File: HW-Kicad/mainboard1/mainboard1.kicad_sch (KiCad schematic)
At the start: 58 parts, among them J1 Conn_01x04_Male, J2 Conn_01x02_Male, J3 Conn_01x07_Male, J4 Conn_01x04_Male, J5 Conn_01x04_Male, J8 Conn_02x10_Odd_Even, Q1 BC337, Q2 IRF9540N, Q3 BC337, Q4 BC337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

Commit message: agegue el conector de energía separado para el aprs
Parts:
- added J6: Conn_01x02_Male, Connector_PinHeader_2.54mm:PinHeader_1x02_P2.54mm_Vertical, symbol Connector:Conn_01x02_Male
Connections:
- net GND: now also J6.2 (Pin_2)
- net VBAT: no longer J2.1 (Pin_1)
- new net APRSBATT: J2.1 (Pin_1), J6.1 (Pin_1)
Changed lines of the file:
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@@
     (stroke (width 0) (type default) (color 0 0 0 0))
   )
-  (polyline (pts (xy 15.24 45.72) (xy 15.24 63.5))
+  (polyline (pts (xy 15.24 30.48) (xy 15.24 63.5))
     (stroke (width 0) (type default) (color 0 0 0 0))
   )
@@
     (stroke (width 0) (type default) (color 0 0 0 0))
   )
-  (polyline (pts (xy 41.91 45.72) (xy 46.99 45.72))
+  (polyline (pts (xy 42.545 30.48) (xy 46.99 30.48))
     (stroke (width 0) (type default) (color 0 0 0 0))
   )
@@
     (stroke (width 0) (type default) (color 0 0 0 0))
   )
-  (polyline (pts (xy 15.24 45.72) (xy 41.91 45.72))
+  (polyline (pts (xy 15.24 30.48) (xy 42.545 30.48))
     (stroke (width 0) (type default) (color 0 0 0 0))
   )
@@
     (stroke (width 0) (type default) (color 0 0 0 0))
   )
-  (polyline (pts (xy 46.99 60.96) (xy 46.99 45.72))
+  (polyline (pts (xy 46.99 60.96) (xy 46.99 30.48))
     (stroke (width 0) (type default) (color 0 0 0 0))
   )
@@
     (effects (font (size 1.27 1.27)) (justify left bottom))
   )
-  (text "Battery Module Input" (at 15.24 45.72 0)
+  (text "Battery Module Input" (at 16.51 16.51 0)
     (effects (font (size 1.27 1.27)) (justify left bottom))
   )
@@
     (effects (font (size 1.27 1.27)) (justify left bottom))
   )
-  (text "4,5 to 10v max" (at 44.45 160.02 0)
+  (text "4,5 to 10v max" (at 44.45 162.56 0)
     (effects (font (size 1.27 1.27)) (justify left bottom))
   )
@@
     )
   )
+  (global_label "APRSBATT" (shape input) (at 29.845 37.465 0) (fields_autoplaced)
+    (effects (font (size 1.27 1.27)) (justify left))
+    (property "Intersheet References" "${INTERSHEET_REFS}" (id 0) (at 41.39 37.3856 0)
+      (effects (font (size 1.27 1.27)) (justify left) hide)
+    )
+  )
   (global_label "SCL" (shape input) (at 128.27 129.54 180) (fields_autoplaced)
     (effects (font (size 1.27 1.27)) (justify right))
@@
     )
   )
-  (global_label "VBAT" (shape input) (at 36.83 158.75 0) (fields_autoplaced)
-    (effects (font (size 1.27 1.27)) (justify left))
-    (property "Intersheet References" "${INTERSHEET_REFS}" (id 0) (at 43.6579 158.6706 0)
-      (effects (font (size 1.27 1.27)) (justify left) hide)
-    )
-  )
   (global_label "PAYLOAD1RX" (shape input) (at 93.98 180.34 0) (fields_autoplaced)
     (effects (font (size 1.27 1.27)) (justify left))
@@
     (effects (font (size 1.27 1.27)) (justify left))
     (property "Intersheet References" "${INTERSHEET_REFS}" (id 0) (at 110.1212 185.4994 0)
+      (effects (font (size 1.27 1.27)) (justify left) hide)
+    )
+  )
+  (global_label "APRSBATT" (shape input) (at 36.83 158.75 0) (fields_autoplaced)
+    (effects (font (size 1.27 1.27)) (justify left))
+    (property "Intersheet References" "${INTERSHEET_REFS}" (id 0) (at 48.375 158.6706 0)
       (effects (font (size 1.27 1.27)) (justify left) hide)
     )
@@
     (pin "2")
     (pin "3")
+    (pin "5")
+    (pin "6")
+    (pin "7")
+    (pin "10")
+    (pin "8")
+    (pin "9")
+    (pin "12")
+    (pin "13")
+    (pin "14")
+    (pin "11")
+    (pin "4")
   )
   (symbol (lib_id "Device:R") (at 358.14 87.63 90) (unit 1)
@@
       (effects (font (size 1.27 1.27)) hide)
     )
+    (pin "1")
+    (pin "2")
+    (pin "3")
+    (pin "4")
+    (pin "5")
+    (pin "6")
+    (pin "10")
+    (pin "8")
+    (pin "9")
     (pin "11")
     (pin "12")
     (pin "13")
+    (pin "14")
+    (pin "7")
   )
   (symbol (lib_id "lm2596:YAAJ_DCDC_StepDown_LM2596") (at 72.39 54.61 0) (unit 1)
@@
       (effects (font (size 1.27 1.27)) hide)
     )
+    (pin "1")
+    (pin "2")
+    (pin "3")
     (pin "4")
     (pin "5")
     (pin "6")
+    (pin "10")
+    (pin "8")
+    (pin "9")
+    (pin "11")
+    (pin "12")
+    (pin "13")
+    (pin "14")
+    (pin "7")
   )
   (symbol (lib_id "power:GND") (at 273.05 234.95 0) (unit 1)
@@
       (effects (font (size 1.27 1.27)) hide)
     )
+    (pin "1")
+    (pin "2")
+    (pin "3")
+    (pin "4")
+    (pin "5")
+    (pin "6")
+    (pin "10")
+    (pin "8")
+    (pin "9")
+    (pin "11")
+    (pin "12")
+    (pin "13")
     (pin "14")
     (pin "7")
@@
       (effects (font (size 1.27 1.27)) hide)
     )
+    (pin "1")
+    (pin "2")
+    (pin "3")
+    (pin "5")
+    (pin "6")
+    (pin "7")
+    (pin "10")
+    (pin "8")
+    (pin "9")
+    (pin "12")
+    (pin "13")
+    (pin "14")
     (pin "11")
     (pin "4")
@@
       (effects (font (size 1.27 1.27)) hide)
     )
+    (pin "1")
+    (pin "2")
+    (pin "3")
     (pin "5")
     (pin "6")
     (pin "7")
+    (pin "10")
+    (pin "8")
+    (pin "9")
+    (pin "12")
+    (pin "13")
+    (pin "14")
+    (pin "11")
+    (pin "4")
   )
   (symbol (lib_id "Connector:Conn_01x02_Male") (at 31.75 158.75 0) (unit 1)
@@
     (pin "2")
     (pin "3")
+    (pin "4")
+    (pin "5")
+    (pin "6")
+    (pin "10")
+    (pin "8")
+    (pin "9")
+    (pin "11")
+    (pin "12")
+    (pin "13")
+    (pin "14")
+    (pin "7")
   )
   (symbol (lib_id "Device:C") (at 369.57 181.61 90) (unit 1)
@@
       (effects (font (size 1.27 1.27)) hide)
     )
+    (pin "1")
+    (pin "2")
+    (pin "3")
+    (pin "5")
+    (pin "6")
+    (pin "7")
+    (pin "10")
+    (pin "8")
+    (pin "9")
     (pin "12")
     (pin "13")
     (pin "14")
+    (pin "11")
+    (pin "4")
   )
   (symbol (lib_id "Device:R") (at 375.92 189.23 180) (unit 1)
@@
     (pin "1")
     (pin "2")
+  )
+  (symbol (lib_id "power:GND") (at 29.845 40.005 0) (unit 1)
+    (in_bom yes) (on_board yes)
+    (property "Reference" "#PWR0133" (id 0) (at 29.845 46.355 0)
+      (effects (font (size 1.27 1.27)) hide)
+    )
+    (property "Value" "GND" (id 1) (at 33.02 42.545 0))
+    (property "Footprint" "" (id 2) (at 29.845 40.005 0)
+      (effects (font (size 1.27 1.27)) hide)
+    )
+    (property "Datasheet" "" (id 3) (at 29.845 40.005 0)
+      (effects (font (size 1.27 1.27)) hide)
+    )
+    (pin "1")
   )
   (symbol (lib_id "power:GND") (at 251.46 109.22 0) (unit 1)
@@
     (pin "2")
   )
+  (symbol (lib_id "Connector:Conn_01x02_Male") (at 24.765 37.465 0) (unit 1)
+    (in_bom yes) (on_board yes) (fields_autoplaced)
+    (property "Reference" "J6" (id 0) (at 25.4 32.385 0))
+    (property "Value" "Conn_01x02_Male" (id 1) (at 25.4 34.925 0))
+    (property "Footprint" "Connector_PinHeader_2.54mm:PinHeader_1x02_P2.54mm_Vertical" (id 2) (at 24.765 37.465 0)
+      (effects (font (size 1.27 1.27)) hide)
+    )
+    (property "Datasheet" "~" (id 3) (at 24.765 37.465 0)
+      (effects (font (size 1.27 1.27)) hide)
+    )
+    (pin "1")
+    (pin "2")
+  )
   (symbol (lib_id "power:GND") (at 264.16 81.28 0) (unit 1)
     (in_bom yes) (on_board yes) (fields_autoplaced)
@@
       (effects (font (size 1.27 1.27)) hide)
     )
+    (pin "1")
+    (pin "2")
+    (pin "3")
+    (pin "4")
+    (pin "5")
+    (pin "6")
     (pin "10")
     (pin "8")
     (pin "9")
+    (pin "11")
+    (pin "12")
+    (pin "13")
+    (pin "14")
+    (pin "7")
   )
   (symbol (lib_id "power:GND") (at 199.39 147.32 0) (unit 1)
@@
       (effects (font (size 1.27 1.27)) hide)
     )
+    (pin "1")
+    (pin "2")
+    (pin "3")
+    (pin "5")
+    (pin "6")
+    (pin "7")
     (pin "10")
     (pin "8")
     (pin "9")
+    (pin "12")
+    (pin "13")
+    (pin "14")
+    (pin "11")
+    (pin "4")
   )
   (symbol (lib_id "Device:C") (at 273.05 104.14 0) (unit 1)
@@
       (reference "#PWR0132") (unit 1) (value "GND") (footprint "")
     )
+    (path "/9f20b7bf-a242-4e3a-9aaa-c06982823dd9"
+      (reference "#PWR0133") (unit 1) (value "GND") (footprint "")
+    )
     (path "/fa0dbe8b-75a2-4a32-9d90-1f26c2f28af8"
       (reference "C1") (unit 1) (value "100n") (footprint "Capacitor_THT:C_Disc_D3.4mm_W2.1mm_P2.50mm")
@@
       (reference "J5") (unit 1) (value "Conn_01x04_Male") (footprint "Connector_Molex:Molex_KK-254_AE-6410-04A_1x04_P2.54mm_Vertical")
     )
+    (path "/a4b50fce-acd4-4bd3-a633-5907c2b83eee"
+      (reference "J6") (unit 1) (value "Conn_01x02_Male") (footprint "Connector_PinHeader_2.54mm:PinHeader_1x02_P2.54mm_Vertical")
+    )
     (path "/fd961731-aa0f-445d-a456-d081fb562681"

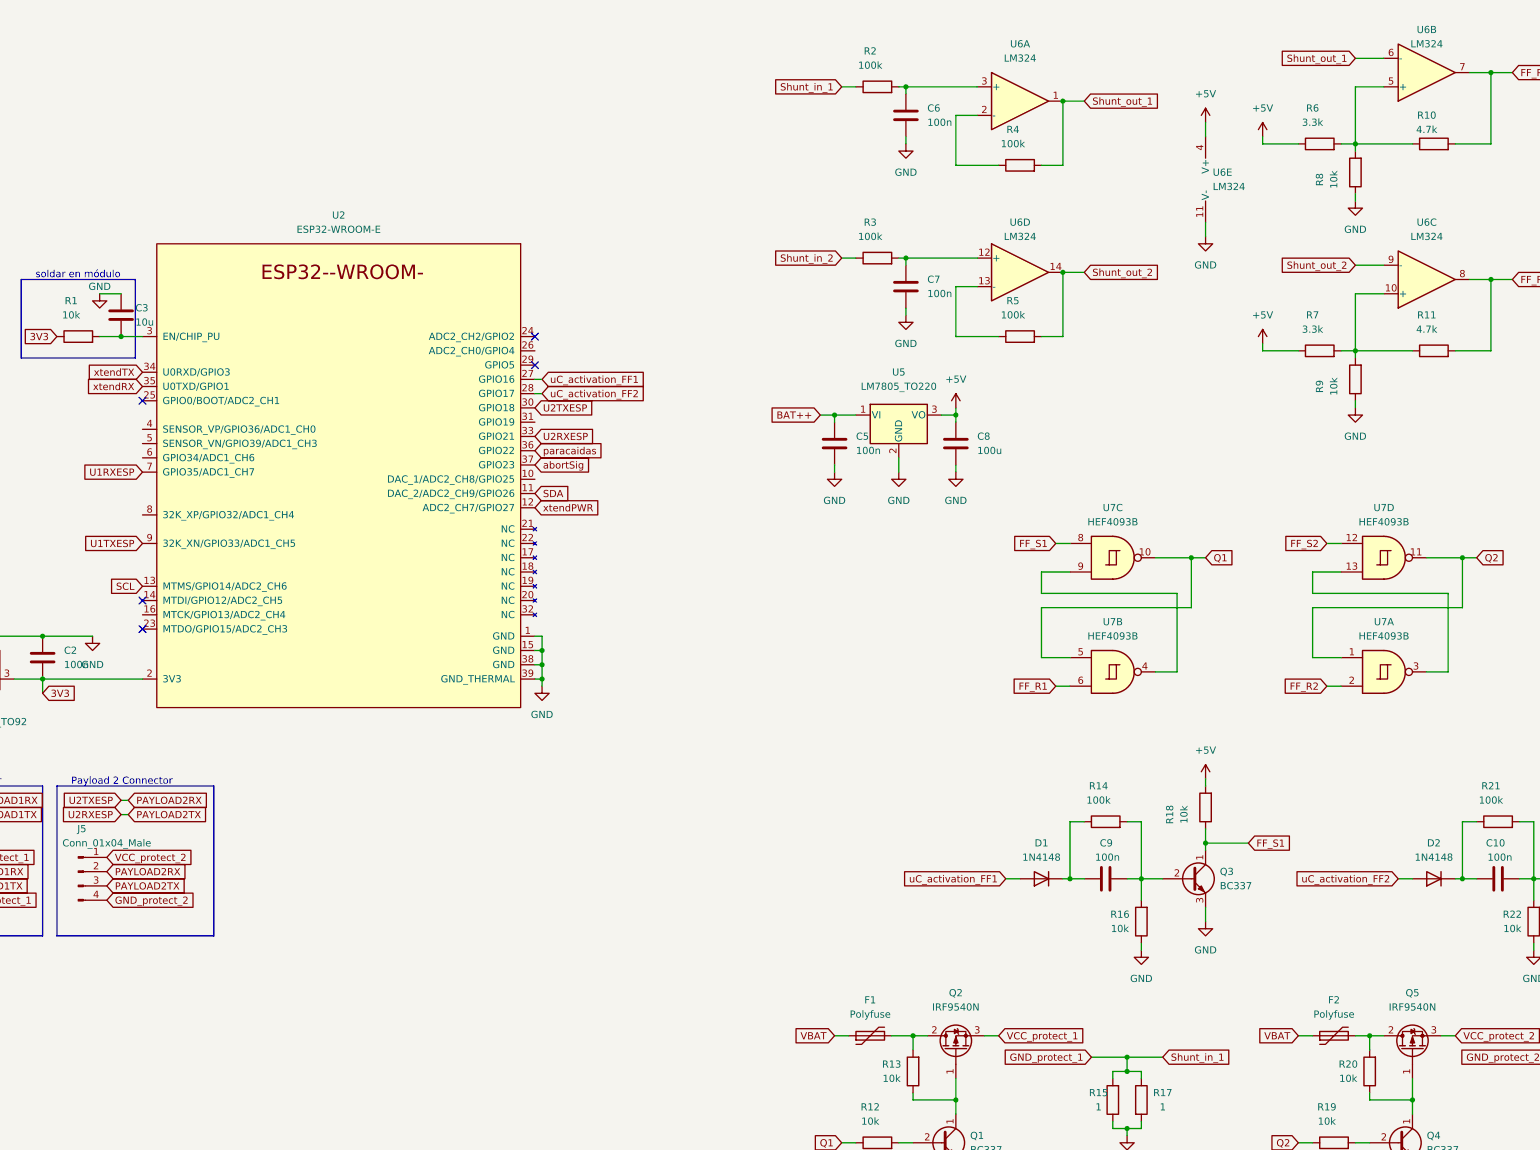
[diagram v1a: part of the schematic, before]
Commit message: correcciones
resistencias en operacionales no inversores de medición de corriente y MOSFET invertidos
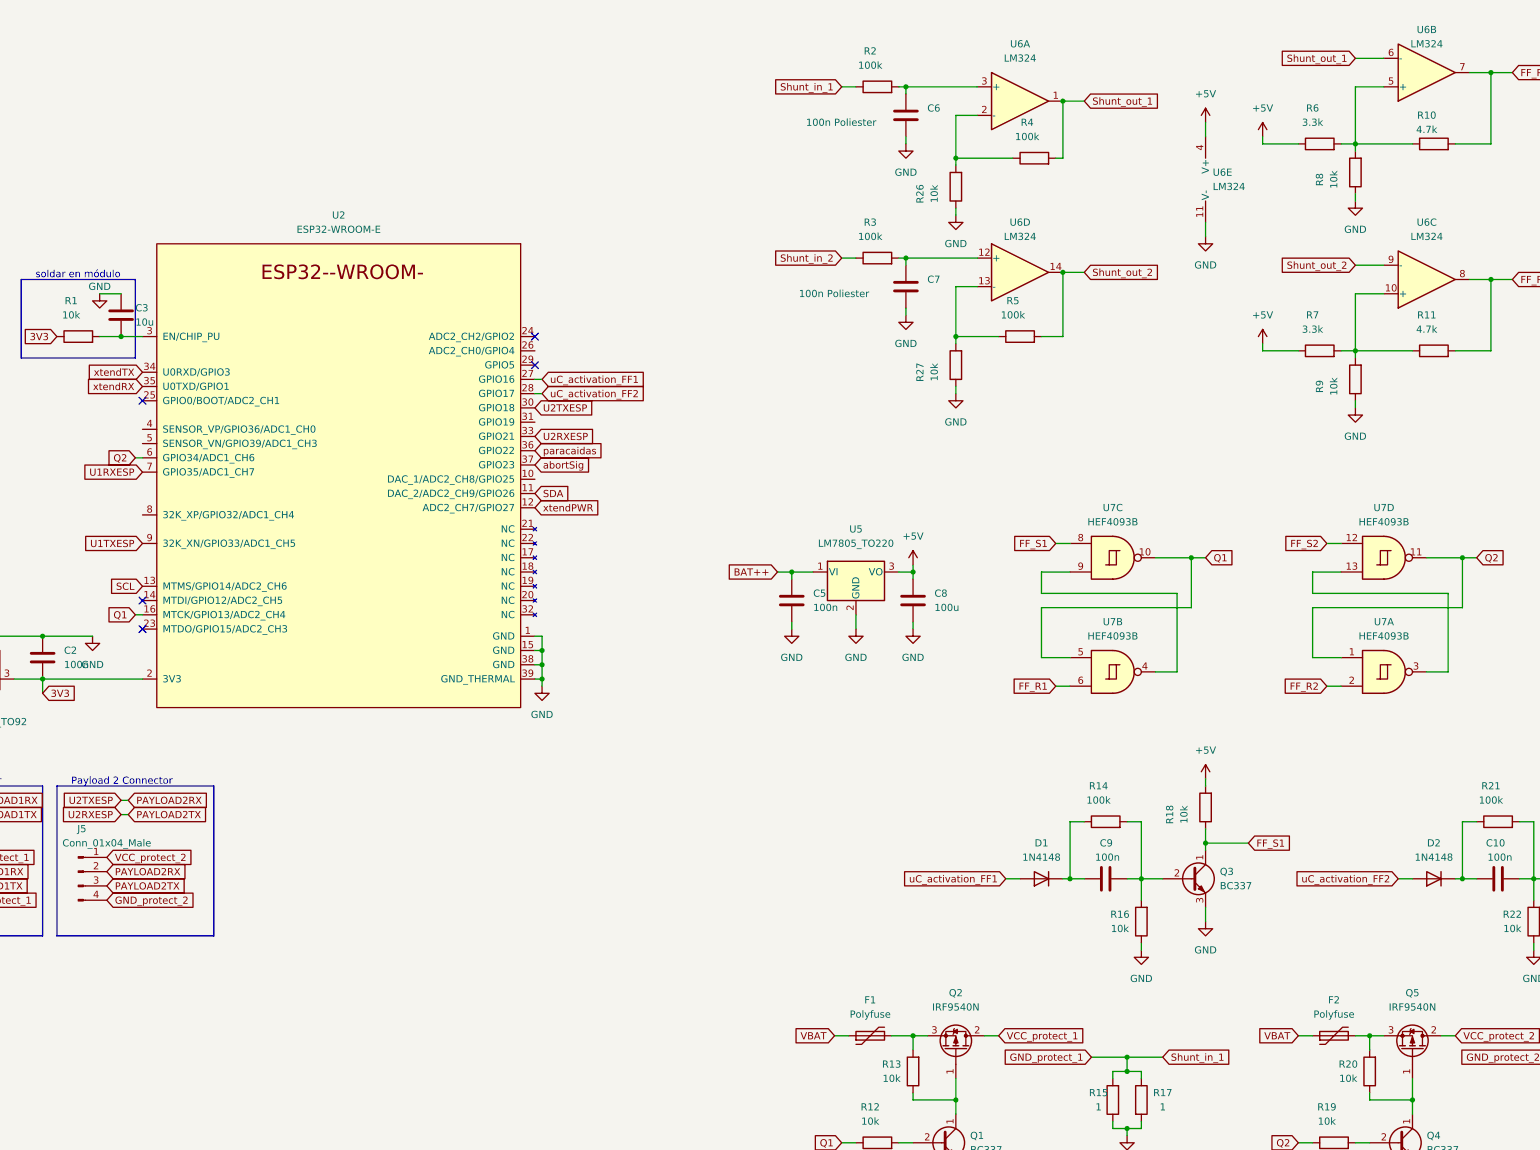
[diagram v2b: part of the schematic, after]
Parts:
- added R26, R27: 10k, Resistor_THT:R_Axial_DIN0207_L6.3mm_D2.5mm_P7.62mm_Horizontal, symbol Device:R
- C6, C7: value 100n -> 100n Poliester
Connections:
- net GND: now also R26.1, R27.1
- net Q1: now also U2.16 (MTCK/GPIO13/ADC2_CH4)
- net Q2: now also U2.6 (GPIO34/ADC1_CH6)
- net VCC_protect_1: now also Q2.2 (D); no longer Q2.3 (S)
- net VCC_protect_2: now also Q5.2 (D); no longer Q5.3 (S)
- net at F1.2, R13.2: now also Q2.3 (S); no longer Q2.2 (D)
- net at R4.1, U6.2 (-): now also R26.2
- net at F2.2, R20.2: now also Q5.3 (S); no longer Q5.2 (D)
- net at R5.1, U6.13 (-): now also R27.2
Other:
- moved on the sheet: C5, C8, Q2, Q5, R4, U5

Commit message: add presentation files
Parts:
- removed HS1: Heatsink, Library:9xtend, symbol Mechanical:Heatsink
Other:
- moved on the sheet: C1, C10, C2, C3, C4, C5, C6, C7, C8, C9, D1, D2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
